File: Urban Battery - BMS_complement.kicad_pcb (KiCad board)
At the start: 2 copper layers, 152.4 x 83.8 mm, 46 parts, among them J1 BMS IO, J10 E-Stop, J11 Contactor Connector, J12 Thermistor, J13 Thermistor, J14 Thermistor, J2 OLED Header, J3 CAN, J4 CAN, J5 Charge Connector, J6 Battery Connector, J7 E-Stop, J8 E-Stop, J9 E-Stop, K1 Charge_Relay, K2 Contactor_Relay, SW1 SW_SPST, SW2 SW_DPDT_x2, SW3 CAN_TERM, U1 MCP2515-I/SO, U2 MCP2561/2, U3 LM2575HVS-12/NOPB, Y1 8MHz

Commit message: only pushing to verify no accidental changes were made before more people work on this again
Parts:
- renumbered locked to REF**

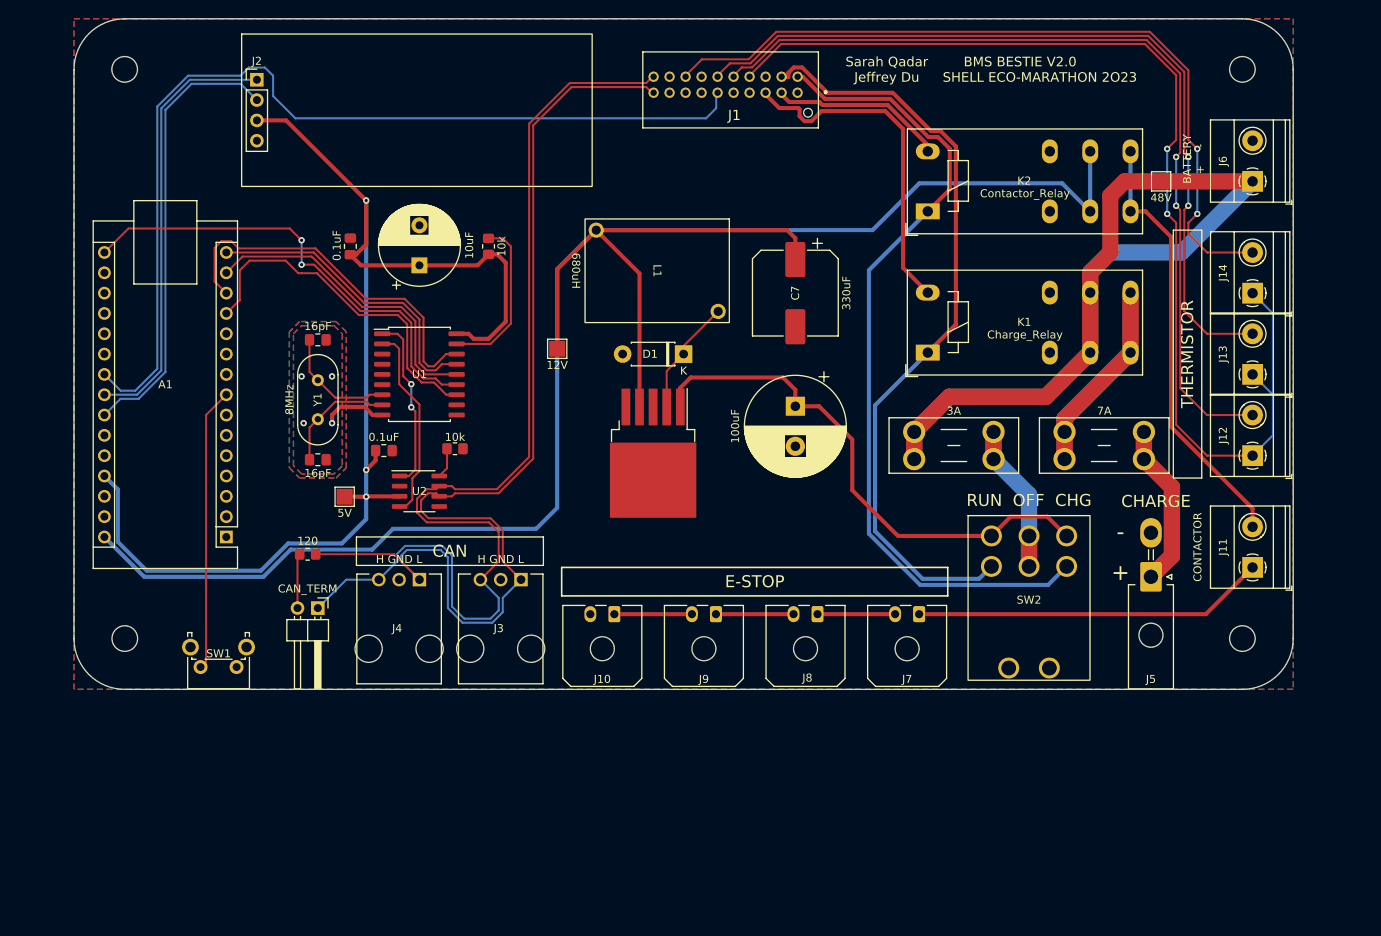
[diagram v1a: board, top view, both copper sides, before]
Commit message: Update footprints for CAN and killswitch connectors
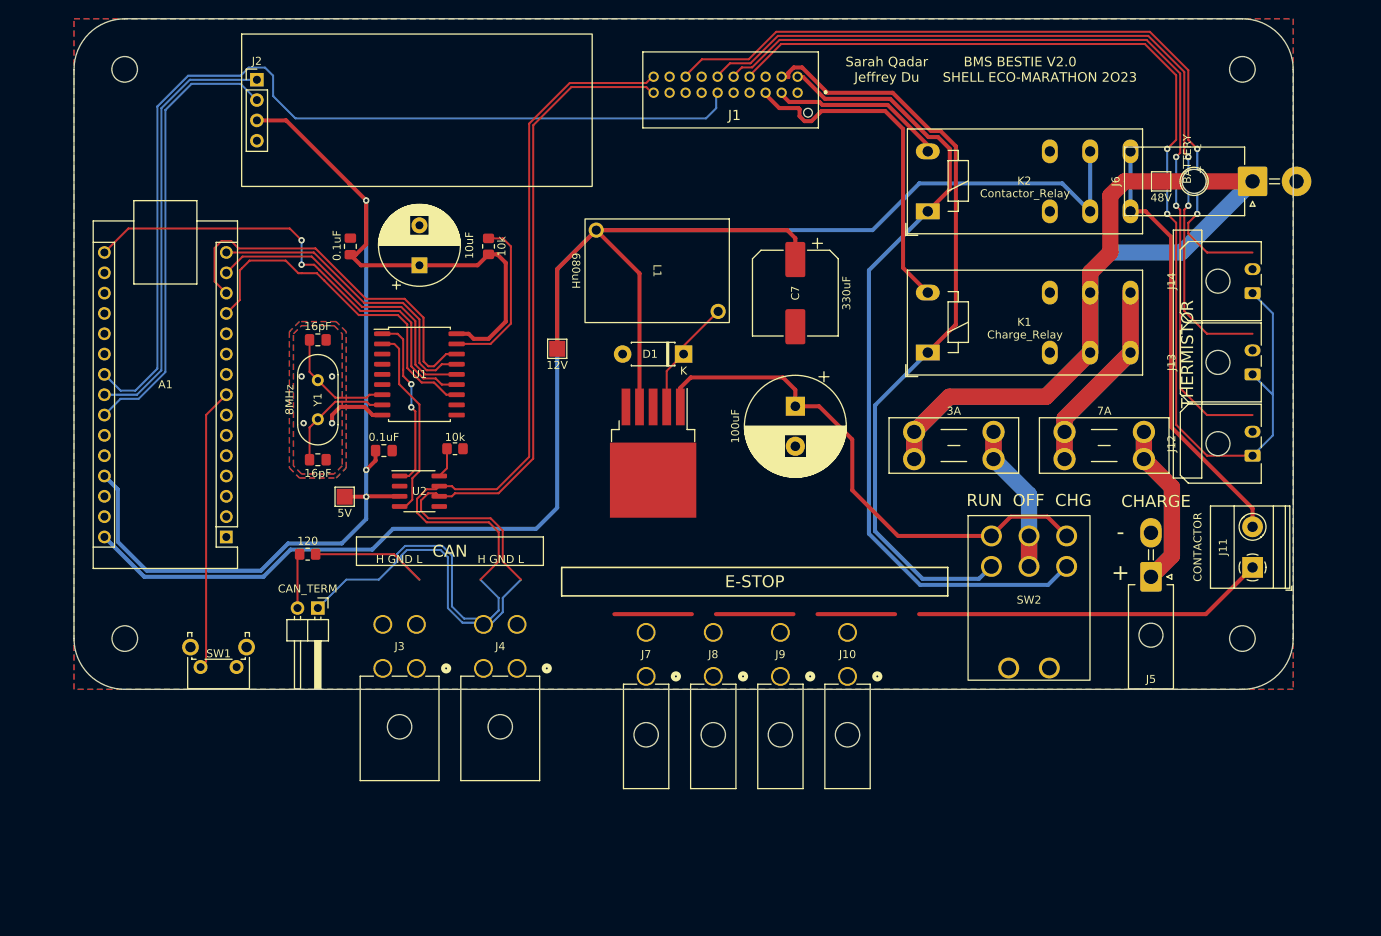
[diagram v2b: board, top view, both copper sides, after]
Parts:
- J10, J7, J8, J9: footprint Connector_Molex:Molex_Micro-Fit_3.0_43650-0200_1x02_P3.00mm_Horizontal -> killswitch_conn_5569_footprints:CONN_5569-02A_MOL
- J12, J13, J14: footprint TerminalBlock_Phoenix:TerminalBlock_Phoenix_MKDS-1,5-2-5.08_1x02_P5.08mm_Horizontal -> Connector_Molex:Molex_Micro-Fit_3.0_43650-0200_1x02_P3.00mm_Horizontal
- J3, J4: footprint BMS_Custom_Footprints:molex-sl-1x03-horizontal -> CAN_conn_5569_footprints:CONN_5569-04A_MOL
- J6: footprint TerminalBlock_Phoenix:TerminalBlock_Phoenix_MKDS-1,5-2-5.08_1x02_P5.08mm_Horizontal -> Connector_Molex:Molex_Mega-Fit_76825-0002_2x01_P5.70mm_Horizontal
- moved J7 35.0 mm to (147.7, 133.0), turned to 0 degrees
- moved J10 30.2 mm to (172.9, 133.0), turned to 0 degrees
- moved J4 15.6 mm to (131.6, 132.0)
- moved J8 15.2 mm to (156.1, 133.0), turned to 0 degrees
- moved J3 11.7 mm to (119.0, 132.0)
- moved J9 11.2 mm to (164.5, 133.0), turned to 0 degrees
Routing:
- net CAN-: track 139.2 -> 109.2 mm
- net CAN+: track 134.9 -> 164.9 mm
- net Net-(J7-Pad2): track 9.70 -> 0.00 mm
- net Net-(J10-Pad1): track 9.70 -> 19.4 mm

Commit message: Revised layout with new test pin & connector footprints, altered board shape
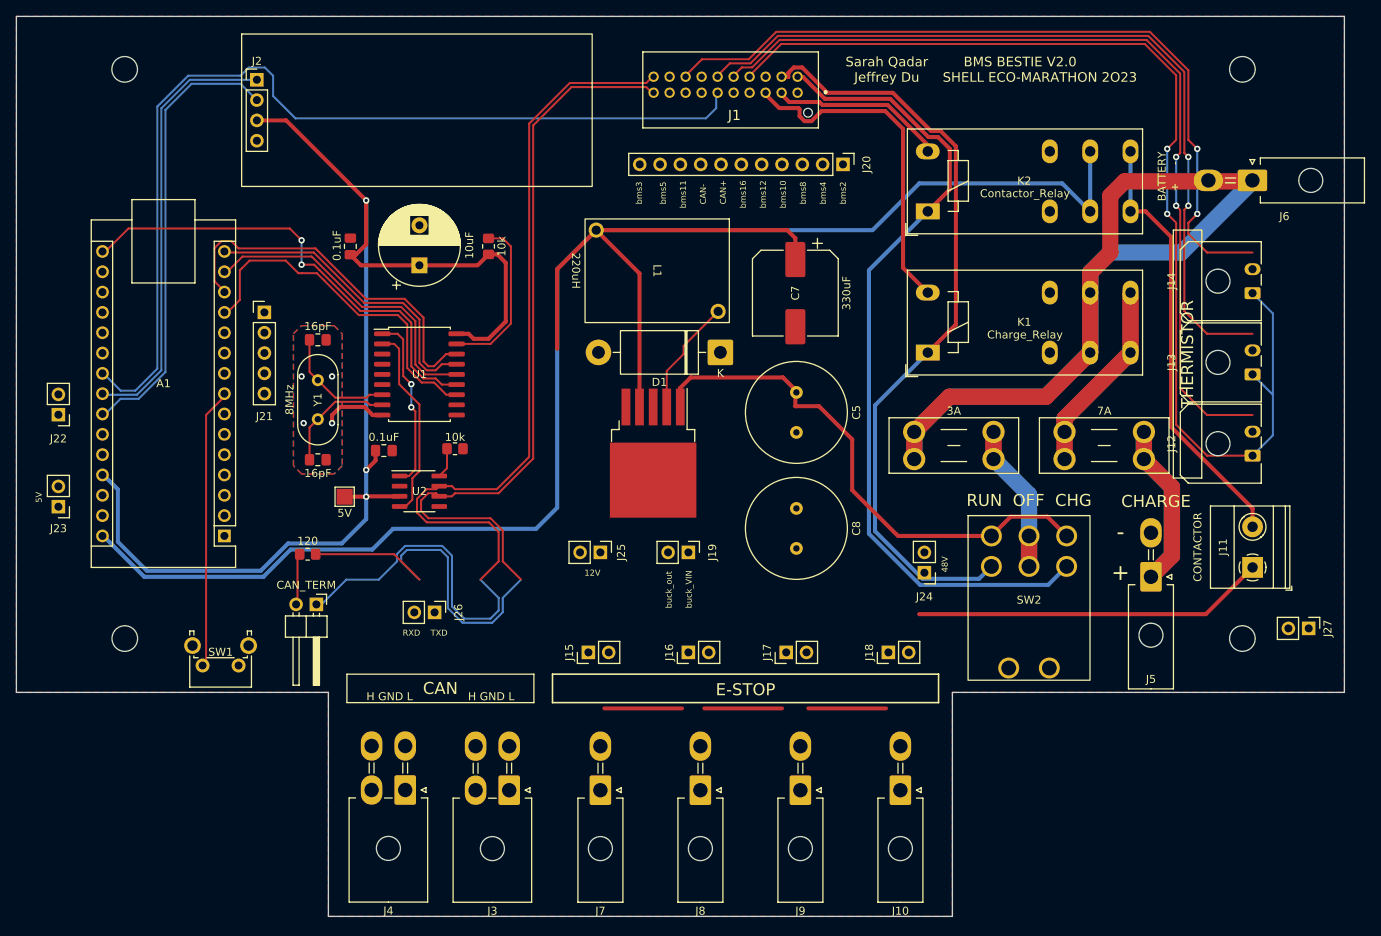
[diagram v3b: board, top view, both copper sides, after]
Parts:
- removed TP2: 48V, TestPoint:TestPoint_Pad_2.0x2.0mm
- removed TP3: 12V, TestPoint:TestPoint_Pad_2.0x2.0mm
- added C8: 220uF, Capacitor_THT:C_Radial_D12.5mm_H25.0mm_P5.00mm, F.Cu at (166.5, 112.0)
- added J15: short pins, Connector_PinHeader_2.54mm:PinHeader_1x02_P2.54mm_Vertical, F.Cu at (140.5, 130.0)
- added J16: short pins, Connector_PinHeader_2.54mm:PinHeader_1x02_P2.54mm_Vertical, F.Cu at (153.0, 130.0)
- added J17: short pins, Connector_PinHeader_2.54mm:PinHeader_1x02_P2.54mm_Vertical, F.Cu at (165.2, 130.0)
- added J18: short pins, Connector_PinHeader_2.54mm:PinHeader_1x02_P2.54mm_Vertical, F.Cu at (178.0, 130.0)
- added J19: Test-pins, Connector_PinHeader_2.54mm:PinHeader_1x02_P2.54mm_Vertical, F.Cu at (153.0, 117.5)
- added J20: Test-pins, Connector_PinHeader_2.54mm:PinHeader_1x11_P2.54mm_Vertical, F.Cu at (172.3, 69.0)
- added J21: Test-pins, Connector_PinHeader_2.54mm:PinHeader_1x05_P2.54mm_Vertical, F.Cu at (100.0, 87.5)
- added J22: Test-pins, Connector_PinHeader_2.54mm:PinHeader_1x02_P2.54mm_Vertical, F.Cu at (74.2, 100.3)
- added J23: Test-pins, Connector_PinHeader_2.54mm:PinHeader_1x02_P2.54mm_Vertical, F.Cu at (74.2, 111.8)
- added J24: Test-pins, Connector_PinHeader_2.54mm:PinHeader_1x02_P2.54mm_Vertical, F.Cu at (182.5, 120.0)
- added J25: Test-pins, Connector_PinHeader_2.54mm:PinHeader_1x02_P2.54mm_Vertical, F.Cu at (142.0, 117.5)
- added J26: Test-pins, Connector_PinHeader_2.54mm:PinHeader_1x02_P2.54mm_Vertical, F.Cu at (121.3, 125.0)
- added J27: Test-pins, Connector_PinHeader_2.54mm:PinHeader_1x02_P2.54mm_Vertical, F.Cu at (230.5, 127.0)
- C5: value 100uF -> 220uF; footprint Capacitor_THT:CP_Radial_D12.5mm_P5.00mm -> Capacitor_THT:C_Radial_D12.5mm_H25.0mm_P5.00mm
- D1: footprint Diode_THT:D_DO-41_SOD81_P7.62mm_Horizontal -> Diode_THT:D_DO-201AD_P15.24mm_Horizontal
- J10, J7, J8, J9: footprint killswitch_conn_5569_footprints:CONN_5569-02A_MOL -> Connector_Molex:Molex_Mini-Fit_Jr_5569-02A2_2x01_P4.20mm_Horizontal
- J3, J4: footprint CAN_conn_5569_footprints:CONN_5569-04A_MOL -> Connector_Molex:Molex_Mini-Fit_Jr_5569-04A2_2x02_P4.20mm_Horizontal
- J6: footprint Connector_Molex:Molex_Mega-Fit_76825-0002_2x01_P5.70mm_Horizontal -> Connector_Molex:Molex_Mini-Fit_Jr_5569-02A2_2x01_P4.20mm_Horizontal
- L1: value 680uH -> 220uH
- U3: value LM2575HVS-12/NOPB -> LM2576HVS-12
- moved G*** 76.6 mm to (83.0, 66.0)
- moved J4 20.7 mm to (117.6, 147.2), turned to 180 degrees
- moved J3 19.1 mm to (130.6, 147.2), turned to 180 degrees
- moved J10 15.7 mm to (179.5, 147.2), turned to 180 degrees
- moved J7 15.3 mm to (142.0, 147.2), turned to 180 degrees
- moved J9 14.4 mm to (167.0, 147.2), turned to 180 degrees
- moved J8 14.3 mm to (154.5, 147.2), turned to 180 degrees
- moved D1 4.60 mm to (157.0, 92.5)
- moved C5 1.74 mm to (166.5, 97.5)
- moved SW3 0.49 mm to (106.5, 124.0)
- moved SW1 0.32 mm to (96.8, 131.6)
- moved A1 0.27 mm to (95.0, 115.4)
- moved J6 0.12 mm to (223.5, 71.0), turned to -90 degrees
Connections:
- net Net-(A1-SCL/A5) renamed SCL
- net Net-(A1-SDA/A4) renamed SDA
- net Net-(D1-K) renamed buck_out
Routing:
- net (no net): track 0.00 -> 29.1 mm
- net Net-(J10-Pin_1): track 19.4 -> 0.00 mm
- net Net-(J16-Pin_2): track 9.70 -> 0.00 mm
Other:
- board size 152.4 x 83.8 mm -> 166 x 112.5 mm
- board text added: "12V"
- board text added: "48V"
- board text added: "5V"
- board text added: "CAN+"
- board text added: "CAN-"
- board text added: "RXD"
- board text added: "TXD"
- board text added: "bms10"
- board text added: "bms11"
- board text added: "bms12"
- board text added: "bms16"
- board text added: "bms2"
- board text added: "bms3"
- board text added: "bms4"
- board text added: "bms5"
- board text added: "bms8"
- board text added: "buck_VIN"
- board text added: "buck_out"

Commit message: Fixed up some more stuff in schematic
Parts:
- removed TP1: 5V, TestPoint:TestPoint_Pad_2.0x2.0mm
- J12, J13, J14: footprint Connector_Molex:Molex_Micro-Fit_3.0_43650-0200_1x02_P3.00mm_Horizontal -> TerminalBlock_Phoenix:TerminalBlock_Phoenix_MKDS-1,5-2-5.08_1x02_P5.08mm_Horizontal
- moved G*** 157.6 mm to (219.1, 145.5)
- moved J24 68.0 mm to (219.5, 63.0), turned to 90 degrees
- moved J22 41.6 mm to (94.2, 63.8)
- moved J26 21.7 mm to (104.5, 111.2), turned to 90 degrees
- moved J23 18.1 mm to (88.2, 123.2), turned to -90 degrees
- moved J25 15.9 mm to (139.2, 101.8), turned to 180 degrees
- moved J27 14.5 mm to (216.5, 130.5), turned to 180 degrees
- moved J10 12.1 mm to (169.0, 141.2)
- moved J18 10.9 mm to (168.5, 124.8)
- moved J19 9.60 mm to (157.5, 109.0), turned to 180 degrees
- moved J7 8.46 mm to (148.0, 141.2)
- moved J9 7.84 mm to (162.0, 141.2)
- moved J15 7.57 mm to (146.0, 124.8)
- moved J17 6.76 mm to (161.0, 124.8)
- moved J8 6.02 mm to (155.0, 141.2)
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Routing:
- net bms8: track 138.6 -> 135.8 mm
- net bms10: track 109.8 -> 107.6 mm
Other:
- board size 166 x 112.5 mm -> 154 x 112.5 mm
- board text added: "VIN"
- board text added: "out"
- board text removed: "buck_VIN"
- board text removed: "buck_out"

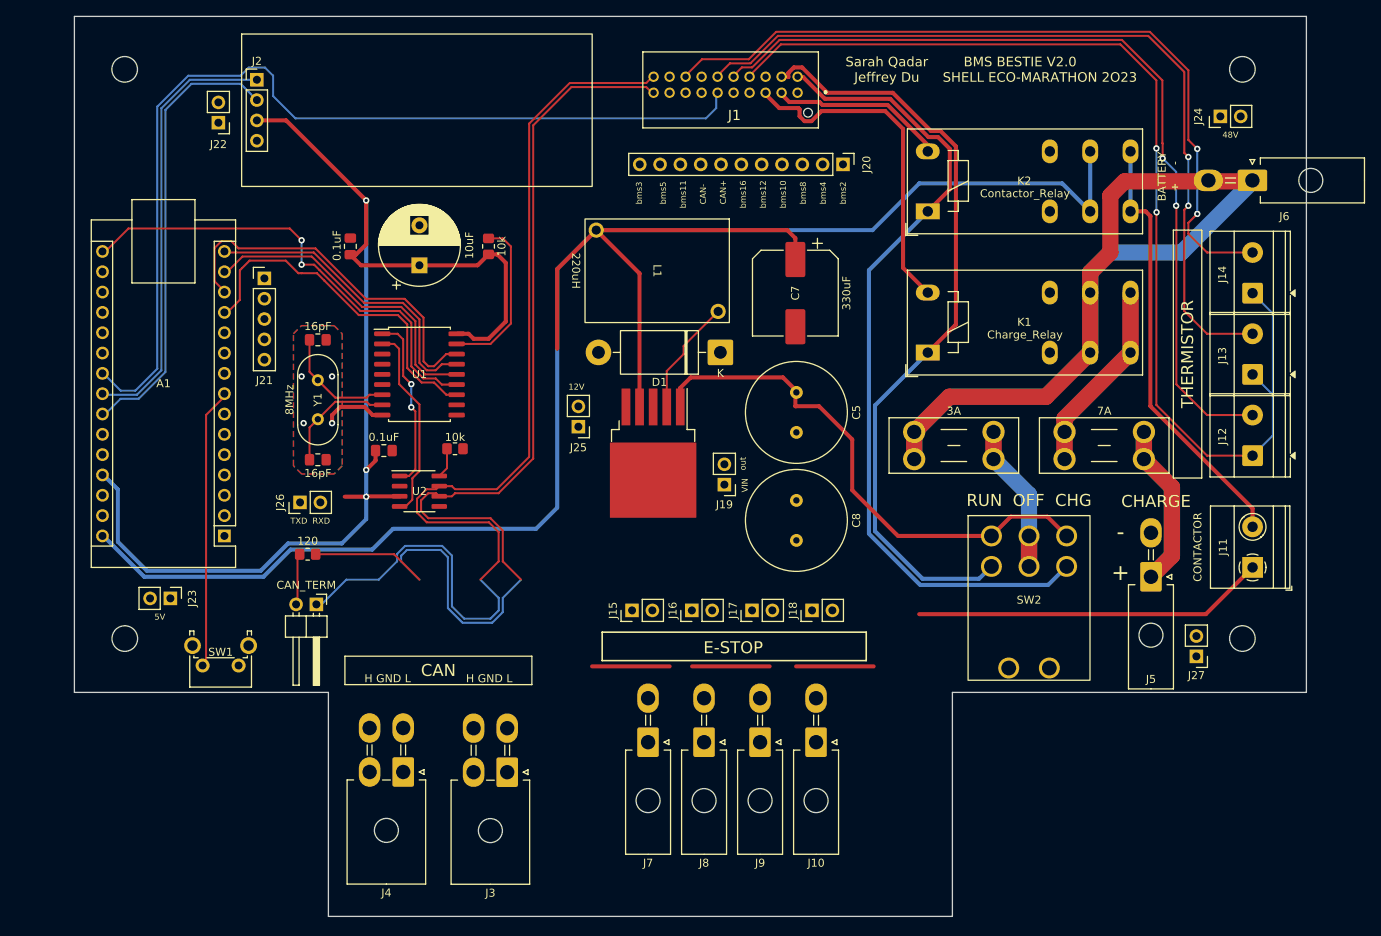
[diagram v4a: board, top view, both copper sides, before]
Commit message: shifted regulator circuit and relay to the left to accomodate new longer minifit connectors. added 48V, 12V, 5V fill zones
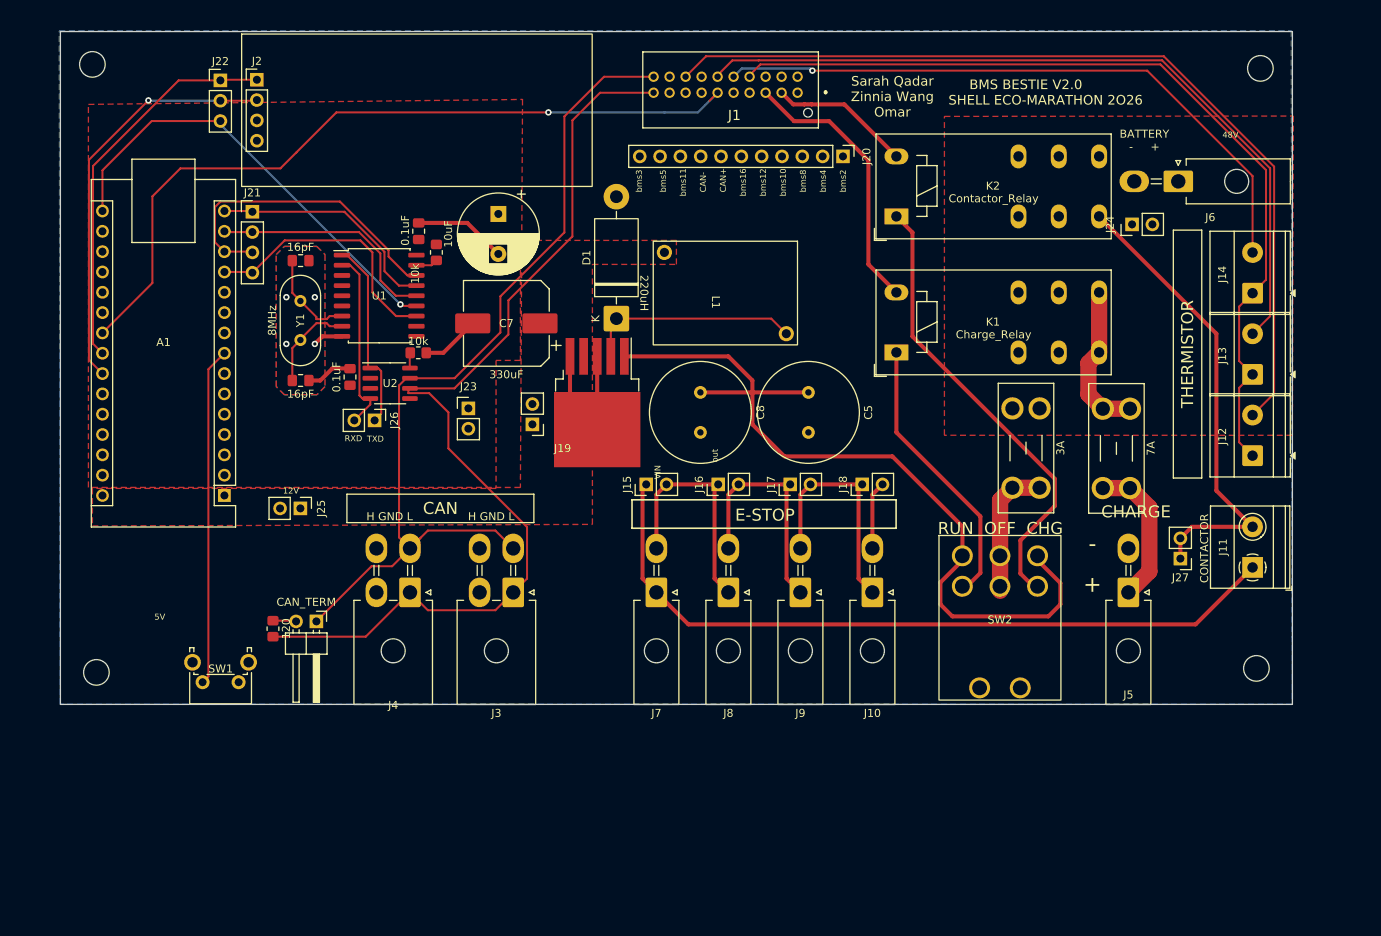
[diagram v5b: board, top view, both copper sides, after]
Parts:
- J21: footprint Connector_PinHeader_2.54mm:PinHeader_1x05_P2.54mm_Vertical -> Connector_PinHeader_2.54mm:PinHeader_1x04_P2.54mm_Vertical
- J22: footprint Connector_PinHeader_2.54mm:PinHeader_1x02_P2.54mm_Vertical -> Connector_PinHeader_2.54mm:PinHeader_1x03_P2.54mm_Vertical
- moved G*** 130.8 mm to (90.8, 119.7)
- moved J23 44.2 mm to (125.5, 99.5), turned to 0 degrees
- moved C7 36.3 mm to (130.2, 88.9), turned to 180 degrees
- moved J25 36.2 mm to (104.5, 112.0), turned to -90 degrees
- moved J19 25.2 mm to (133.5, 101.5)
- moved J3 22.5 mm to (131.1, 122.5)
- moved J4 22.5 mm to (118.2, 122.5)
- moved J10 20.0 mm to (176.0, 122.5)
- moved J9 19.4 mm to (167.0, 122.5)
- moved J8 19.0 mm to (158.0, 122.5)
- moved J7 18.8 mm to (149.0, 122.5)
- moved C8 18.1 mm to (154.5, 97.5)
- moved J24 17.4 mm to (208.5, 76.5)
- moved J18 17.0 mm to (174.7, 109.0)
- moved J17 16.5 mm to (165.7, 109.0)
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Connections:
- J12 pad 2: bms10 -> bms16
- J14 pad 2: bms16 -> bms10
- J22 pad 1: SCL -> SDA
- J22 pad 2: SDA -> SCL
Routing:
- net +12V: track 241.2 -> 0.00 mm
- net +5V: track 155.2 -> 0.00 mm, vias 3 -> 0
- net +48V: track 133.2 -> 0.00 mm
- net bms4: track 96.8 -> 35.1 mm
- net CAN+: track 164.9 -> 112.0 mm
- net Net-(J11-Pin_1): track 44.1 -> 93.5 mm
- net GND: track 8.13 -> 56.7 mm
- net bms2: track 103.5 -> 57.7 mm
- net Buck_VIN: track 66.3 -> 101.6 mm
- net Net-(J16-Pin_2): track 0.00 -> 29.4 mm
- net Net-(J15-Pin_2): track 0.00 -> 29.4 mm
- net Net-(J10-Pin_1): track 0.00 -> 29.4 mm
- net Charge_In: track 48.5 -> 19.2 mm
- net (no net): track 29.1 -> 0.00 mm
- net bms10: track 107.6 -> 81.3 mm, vias 2 -> 1
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- added copper zone on F.Cu, net +12V
- added copper zone on F.Cu, net +48V
- added copper zone on F.Cu, net +5V
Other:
- board size 154 x 112.5 mm -> 154 x 84.1 mm
- board text added: "BATTERY - +"
- board text added: "BMS BESTIE V2.0 SHELL ECO-MARATHON 2O26"
- board text added: "Sarah Qadar Zinnia Wang Omar"
- board text removed: "BATTERY + -"
- board text removed: "BMS BESTIE V2.0 SHELL ECO-MARATHON 2O23"
- board text removed: "Sarah Qadar Jeffrey Du"
